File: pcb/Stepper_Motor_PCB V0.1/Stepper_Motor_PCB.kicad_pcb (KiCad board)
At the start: 2 copper layers, 29 parts, among them J1 Pwr/Coms, J2 Pot, J3 Bootloader Pins, J4 Stepper_Motor, J5 LED, J7 8P8C, SW1 SW_Push, U1 ATmega328P-AU, Y1 Crystal

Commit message: Traced Stepper Motor PCB
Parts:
- moved R8 68.5 mm to (152.4, 76.8), turned to 90 degrees
- moved R6 64.9 mm to (147.8, 76.8), turned to 90 degrees
- moved Rx 64.2 mm to (152.4, 80.3), turned to 90 degrees
- moved R7 62.5 mm to (143.2, 76.8), turned to 90 degrees
- moved 5V 60.4 mm to (147.8, 80.3), turned to 90 degrees
- moved Tx 57.8 mm to (143.2, 80.3), turned to 90 degrees
- moved SW1 53.9 mm to (137.5, 87.7)
- moved J3 26.6 mm to (159.3, 117.7), turned to -90 degrees
- moved J5 8.09 mm to (132.8, 125.2), turned to -90 degrees
- moved R5 4.52 mm to (152.4, 88.8)
- moved J2 4.28 mm to (105.2, 101.9), turned to 0 degrees
- moved C6 2.60 mm to (152.4, 91.6), turned to 0 degrees
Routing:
- net GND: track 0.00 -> 263.8 mm, vias 0 -> 4
- net +5V: track 0.00 -> 196.8 mm, vias 0 -> 3
- net /TXD: track 0.00 -> 93.3 mm, vias 0 -> 1
- net /RXD: track 0.00 -> 88.1 mm
- net /pot: track 0.00 -> 70.5 mm, vias 0 -> 2
- net /SCL: track 0.00 -> 61.1 mm
- net /SDA: track 0.00 -> 60.6 mm
- net /Step: track 0.00 -> 56.4 mm, vias 0 -> 1
- net /Reset: track 0.00 -> 50.9 mm, vias 0 -> 2
- net /Enable: track 0.00 -> 50.1 mm, vias 0 -> 1
- net /Dir: track 0.00 -> 49.6 mm, vias 0 -> 1
- net +12V: track 0.00 -> 40.0 mm
- net /LED: track 0.00 -> 28.1 mm
- net /SCK: track 0.00 -> 25.7 mm
- net /MOSI: track 0.00 -> 19.6 mm
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- added copper zone on F.Cu, net GND
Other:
- board outline added: 97.3 x 58 mm
- board text added: "+5V"
- board text added: "GND"
- board text added: "MISO"
- board text added: "MOSI"
- board text added: "RESET"
- board text added: "SCK"
- board text removed: "Ethernet and Pwr/Coms connectors need to be on the right edge of the board."
- board text removed: "LED connector needs to be on the bottom of the board."
- board text removed: "Stepper Motor and Pot Connectors need to be on the left edge of the board."
- board text removed: "You can place these componets where ever you feel they fit best."

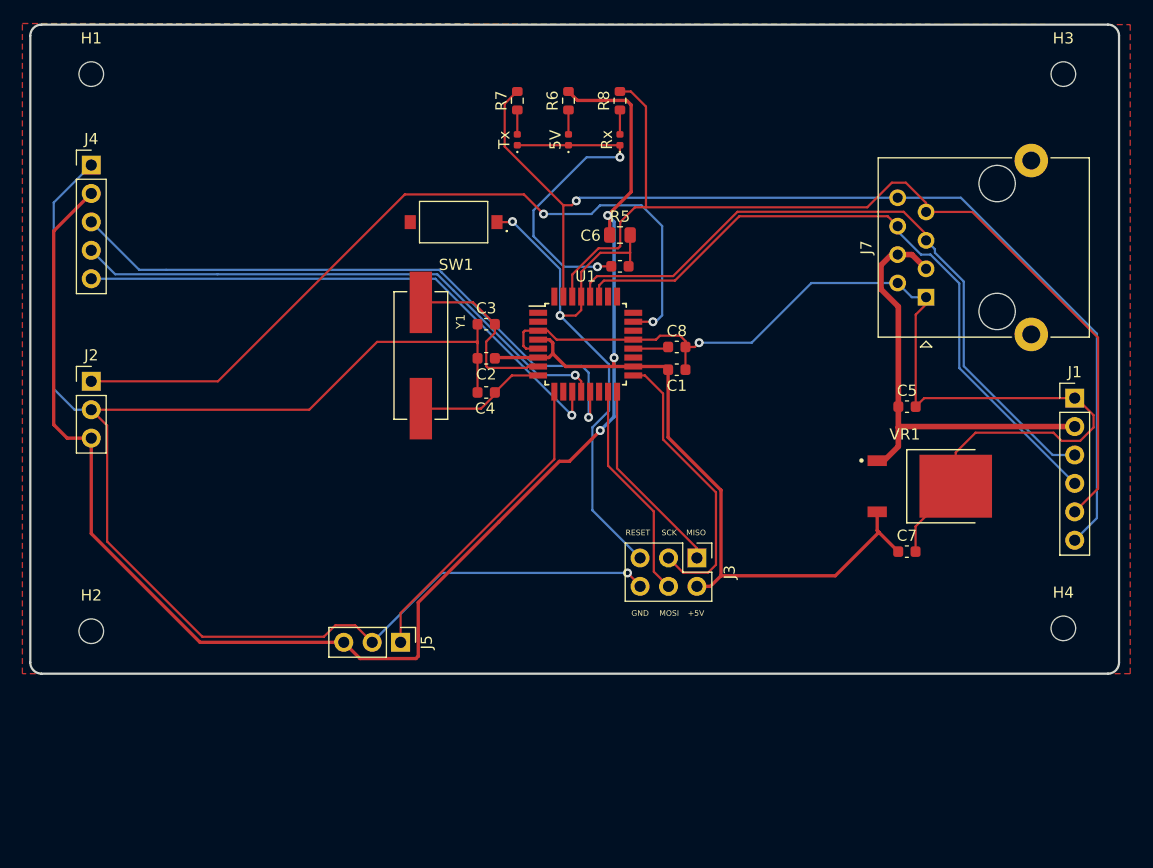
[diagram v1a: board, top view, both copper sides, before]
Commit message: Made PCB smaller
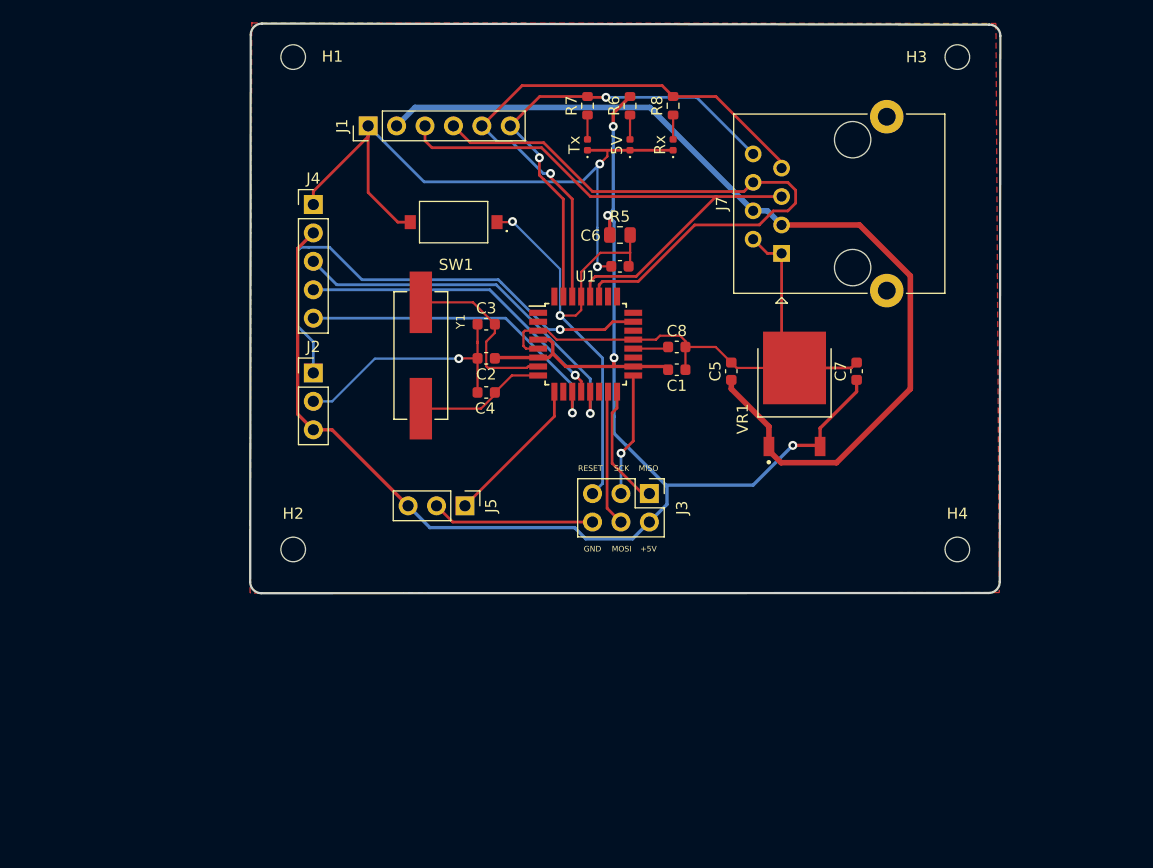
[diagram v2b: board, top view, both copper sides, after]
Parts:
- moved J1 67.7 mm to (129.9, 79.0), turned to 90 degrees
- moved J4 20.2 mm to (125.0, 86.1)
- moved J2 19.9 mm to (125.0, 101.1)
- moved H2 19.5 mm to (123.2, 116.9)
- moved H1 18.1 mm to (123.2, 72.9)
- moved C7 16.7 mm to (173.6, 101.0), turned to 90 degrees
- moved C5 16.0 mm to (162.3, 101.0), turned to 90 degrees
- moved VR1 14.6 mm to (168.0, 103.0), turned to 90 degrees
- moved J7 13.5 mm to (166.8, 90.4)
- moved J5 13.5 mm to (138.6, 113.0)
- moved H4 11.8 mm to (182.6, 116.9)
- moved H3 9.60 mm to (182.6, 72.9)
- moved J3 7.15 mm to (155.0, 111.9)
- moved R7 6.29 mm to (149.5, 77.2)
- moved Tx 6.29 mm to (149.5, 80.7)
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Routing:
- net GND: track 263.8 -> 150.4 mm, vias 4 -> 3
- net +5V: track 196.8 -> 139.0 mm, vias 3 -> 4
- net /TXD: track 93.3 -> 42.1 mm, vias 1 -> 2
- net +12V: track 40.0 -> 86.5 mm
- net /RXD: track 88.1 -> 51.3 mm, vias 0 -> 1
- net /pot: track 70.5 -> 45.0 mm, vias 2 -> 1
- net /Step: track 56.4 -> 34.1 mm
- net /Dir: track 49.6 -> 28.3 mm
- net /Enable: track 50.1 -> 30.0 mm
- net /SCK: track 25.7 -> 11.0 mm, vias 0 -> 1
- net /LED: track 28.1 -> 13.5 mm
- net /SCL: track 61.1 -> 51.0 mm
- net /Reset: track 50.9 -> 42.9 mm
- net /MOSI: track 19.6 -> 12.2 mm
- net /MISO: track 17.8 -> 11.0 mm
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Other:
- board size 97.3 x 58 mm -> 67 x 50.9 mm
- board text removed: "This needs to be in the configuration, try not to move around the componets in this box. (The pullup resistor on the reset pin can be move around slightly, if you want.)"

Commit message: update pcb
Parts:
- moved H4 4.41 mm to (178.8, 114.5)
- moved H3 3.70 mm to (178.8, 73.0)
- moved H2 3.06 mm to (125.1, 114.5)
- moved H1 1.80 mm to (125.0, 72.9)
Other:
- board size 67 x 50.9 mm -> 60 x 47.8 mm
- board text added: "12V"
- board text added: "5V"
- board text added: "DIR"
- board text added: "ENA"
- board text added: "EasyDrift - Stepper Motor Controller V1.0"
- board text added: "LED"
- board text added: "Pot"
- board text added: "RX"
- board text added: "SCL"
- board text added: "SDA"
- board text added: "STEP"
- board text added: "TX"
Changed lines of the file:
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@@
   )
   (footprint "MountingHole:MountingHole_2.2mm_M2" (layer "F.Cu")
-    (at 123.2 116.9)
+    (at 125.1 114.5)
     (descr "Mounting Hole 2.2mm, no annular, M2")
     (tags "mounting hole 2.2mm no annular m2")
@@
     (property "Sheetname" "")
     (attr exclude_from_pos_files)
-    (fp_text reference "H2" (at 0 -3.2) (layer "F.SilkS")
+    (fp_text reference "H2" (at 0 -3.2) (layer "F.SilkS") hide
       (effects (font (size 1 1) (thickness 0.15)))
     )
@@
   )
   (footprint "MountingHole:MountingHole_2.2mm_M2" (layer "F.Cu")
-    (at 182.55 72.9)
+    (at 178.85 73)
     (descr "Mounting Hole 2.2mm, no annular, M2")
     (tags "mounting hole 2.2mm no annular m2")
@@
     (property "Sheetname" "")
     (attr exclude_from_pos_files)
-    (fp_text reference "H3" (at -3.65 0) (layer "F.SilkS")
+    (fp_text reference "H3" (at -3.65 0) (layer "F.SilkS") hide
       (effects (font (size 1 1) (thickness 0.15)))
     )
@@
   )
   (footprint "MountingHole:MountingHole_2.2mm_M2" (layer "F.Cu")
-    (at 182.55 116.9)
+    (at 178.85 114.5)
     (descr "Mounting Hole 2.2mm, no annular, M2")
     (tags "mounting hole 2.2mm no annular m2")
@@
     (property "Sheetname" "")
     (attr exclude_from_pos_files)
-    (fp_text reference "H4" (at 0 -3.2) (layer "F.SilkS")
+    (fp_text reference "H4" (at 0 -3.2) (layer "F.SilkS") hide
       (effects (font (size 1 1) (thickness 0.15)))
     )
@@
   )
   (footprint "MountingHole:MountingHole_2.2mm_M2" (layer "F.Cu")
-    (at 123.2 72.9)
+    (at 125 72.9)
     (descr "Mounting Hole 2.2mm, no annular, M2")
     (tags "mounting hole 2.2mm no annular m2")
@@
     (property "Sheetname" "")
     (attr exclude_from_pos_files)
-    (fp_text reference "H1" (at 3.5 -0.05) (layer "F.SilkS")
+    (fp_text reference "H1" (at 3.5 -0.05) (layer "F.SilkS") hide
       (effects (font (size 1 1) (thickness 0.15)))
     )
@@
     )
   )
-  (gr_line (start 185.342893 120.792893) (end 120.357107 120.810661) (layer "Edge.Cuts") (width 0.2))
-  (gr_line (start 119.357107 119.810661) (end 119.407107 70.907107) (layer "Edge.Cuts") (width 0.2))
-  (gr_arc (start 185.392893 70) (mid 186.1 70.292893) (end 186.392893 71) (layer "Edge.Cuts") (width 0.2))
-  (gr_arc (start 119.407107 70.907107) (mid 119.700001 70.200003) (end 120.407107 69.907107) (layer "Edge.Cuts") (width 0.2))
-  (gr_line (start 186.392893 71) (end 186.342893 119.792893) (layer "Edge.Cuts") (width 0.2))
-  (gr_line (start 120.407107 69.907107) (end 185.392893 70) (layer "Edge.Cuts") (width 0.2))
-  (gr_arc (start 120.357107 120.810661) (mid 119.649996 120.51777) (end 119.357107 119.810661) (layer "Edge.Cuts") (width 0.2))
-  (gr_arc (start 186.342893 119.792893) (mid 186.05 120.5) (end 185.342893 120.792893) (layer "Edge.Cuts") (width 0.2))
-  (gr_rect (start 128.257 83.312) (end 160.261 108.966) (layer "User.1") (width 0.5) (fill none))
+  (gr_line (start 180.992893 117.692891) (end 123.007111 117.717768) (layer "Edge.Cuts") (width 0.2))
+  (gr_line (start 122.007111 116.742893) (end 122.05 70.907107) (layer "Edge.Cuts") (width 0.2))
+  (gr_arc (start 181.05 70) (mid 181.757111 70.292891) (end 182.05 71) (layer "Edge.Cuts") (width 0.2))
+  (gr_arc (start 122.05 70.907107) (mid 122.342891 70.199998) (end 123.05 69.907107) (layer "Edge.Cuts") (width 0.2))
+  (gr_line (start 182.05 71) (end 181.992893 116.692891) (layer "Edge.Cuts") (width 0.2))
+  (gr_line (start 123.05 69.907107) (end 181.05 70) (layer "Edge.Cuts") (width 0.2))
+  (gr_arc (start 123.007111 117.717768) (mid 122.301554 117.441185) (end 122.007111 116.742893) (layer "Edge.Cuts") (width 0.2))
+  (gr_arc (start 181.992893 116.692891) (mid 181.700002 117.4) (end 180.992893 117.692891) (layer "Edge.Cuts") (width 0.2))
   (gr_text "MOSI" (at 152.55 116.85) (layer "F.SilkS")
     (effects (font (size 0.5 0.5) (thickness 0.125)))
   )
+  (gr_text "ENA" (at 128.85 96.3) (layer "F.SilkS")
+    (effects (font (size 1 1) (thickness 0.15)))
+  )
+  (gr_text "GND" (at 128.5 86.1) (layer "F.SilkS")
+    (effects (font (size 1 1) (thickness 0.15)))
+  )
   (gr_text "RESET" (at 149.75 109.65) (layer "F.SilkS")
     (effects (font (size 0.5 0.5) (thickness 0.125)))
   )
+  (gr_text "STEP" (at 128.95 91.25) (layer "F.SilkS")
+    (effects (font (size 1 1) (thickness 0.15)))
+  )
   (gr_text "MISO" (at 154.95 109.65) (layer "F.SilkS")
     (effects (font (size 0.5 0.5) (thickness 0.125)))
   )
+  (gr_text "Pot" (at 128.4 101.05) (layer "F.SilkS")
+    (effects (font (size 1 1) (thickness 0.15)))
+  )
+  (gr_text "SDA" (at 137.6 81.9) (layer "F.SilkS")
+    (effects (font (size 0.75 0.75) (thickness 0.15)))
+  )
+  (gr_text "GND" (at 135.9 115.9) (layer "F.SilkS")
+    (effects (font (size 1 1) (thickness 0.15)))
+  )
+  (gr_text "GND" (at 128.4 103.8) (layer "F.SilkS")
+    (effects (font (size 1 1) (thickness 0.15)))
+  )
+  (gr_text "SCL" (at 134.95 81.9) (layer "F.SilkS")
+    (effects (font (size 0.75 0.75) (thickness 0.15)))
+  )
+  (gr_text "EasyDrift - Stepper Motor Controller V1.0" (at 155.7 72.9) (layer "F.SilkS")
+    (effects (font (size 1 1) (thickness 0.15)))
+  )
+  (gr_text "5V" (at 132.8 115.95) (layer "F.SilkS")
+    (effects (font (size 1 1) (thickness 0.15)))
+  )
+  (gr_text "LED" (at 139.35 115.9) (layer "F.SilkS")
+    (effects (font (size 1 1) (thickness 0.15)))
+  )
+  (gr_text "5V" (at 128.5 106.25) (layer "F.SilkS")
+    (effects (font (size 1 1) (thickness 0.15)))
+  )
+  (gr_text "TX" (at 142.65 81.85) (layer "F.SilkS")
+    (effects (font (size 0.75 0.75) (thickness 0.15)))
+  )
+  (gr_text "DIR" (at 128.95 93.75) (layer "F.SilkS")
+    (effects (font (size 1 1) (thickness 0.15)))
+  )
+  (gr_text "12V" (at 132.4 81.95) (layer "F.SilkS")
+    (effects (font (size 0.75 0.75) (thickness 0.15)))
+  )
   (gr_text "SCK" (at 152.55 109.65) (layer "F.SilkS")
     (effects (font (size 0.5 0.5) (thickness 0.125)))
   )
+  (gr_text "5V" (at 128.5 88.65) (layer "F.SilkS")
+    (effects (font (size 1 1) (thickness 0.15)))
+  )
   (gr_text "+5V" (at 154.95 116.85) (layer "F.SilkS")
     (effects (font (size 0.5 0.5) (thickness 0.125)))
+  )
+  (gr_text "GND" (at 129.6 82) (layer "F.SilkS")
+    (effects (font (size 0.75 0.75) (thickness 0.15)))
+  )
+  (gr_text "RX" (at 140.15 81.85) (layer "F.SilkS")
+    (effects (font (size 0.75 0.75) (thickness 0.15)))
   )
   (gr_text "GND" (at 149.95 116.85) (layer "F.SilkS")
@@
       (pts
         (xy 119.5 69.85)
-        (xy 186 69.9)
-        (xy 186.3 120.75)
+        (xy 182.889052 69.918354)
+        (xy 183.189052 120.768354)
         (xy 119.35 120.8)
         (xy 119.5 69.8)
